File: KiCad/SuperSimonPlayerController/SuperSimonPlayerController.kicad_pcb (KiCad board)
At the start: 2 copper layers, 6 parts, among them U1 ESP32-S3-MINI-1-N8

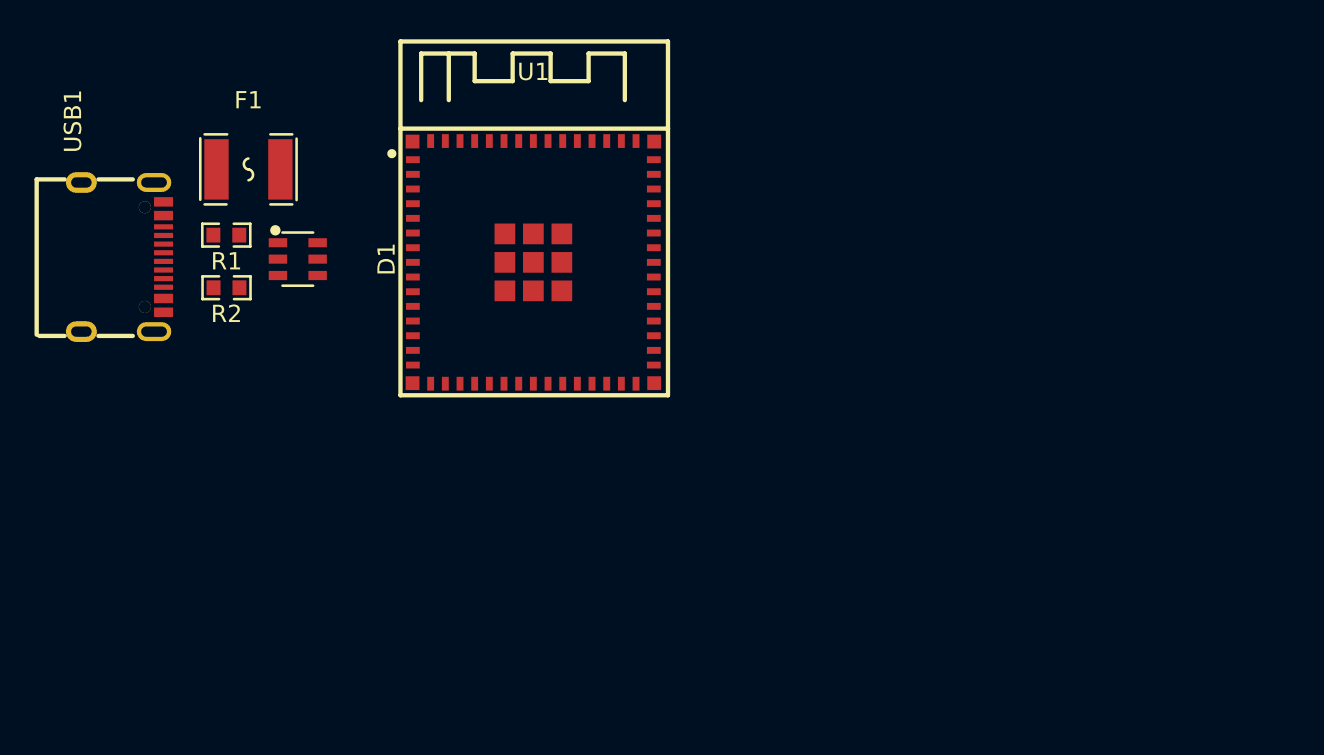
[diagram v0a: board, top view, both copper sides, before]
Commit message: Swapped to esp32-c3 with castallated pads, added some passives, created schematic sheet for the esp32
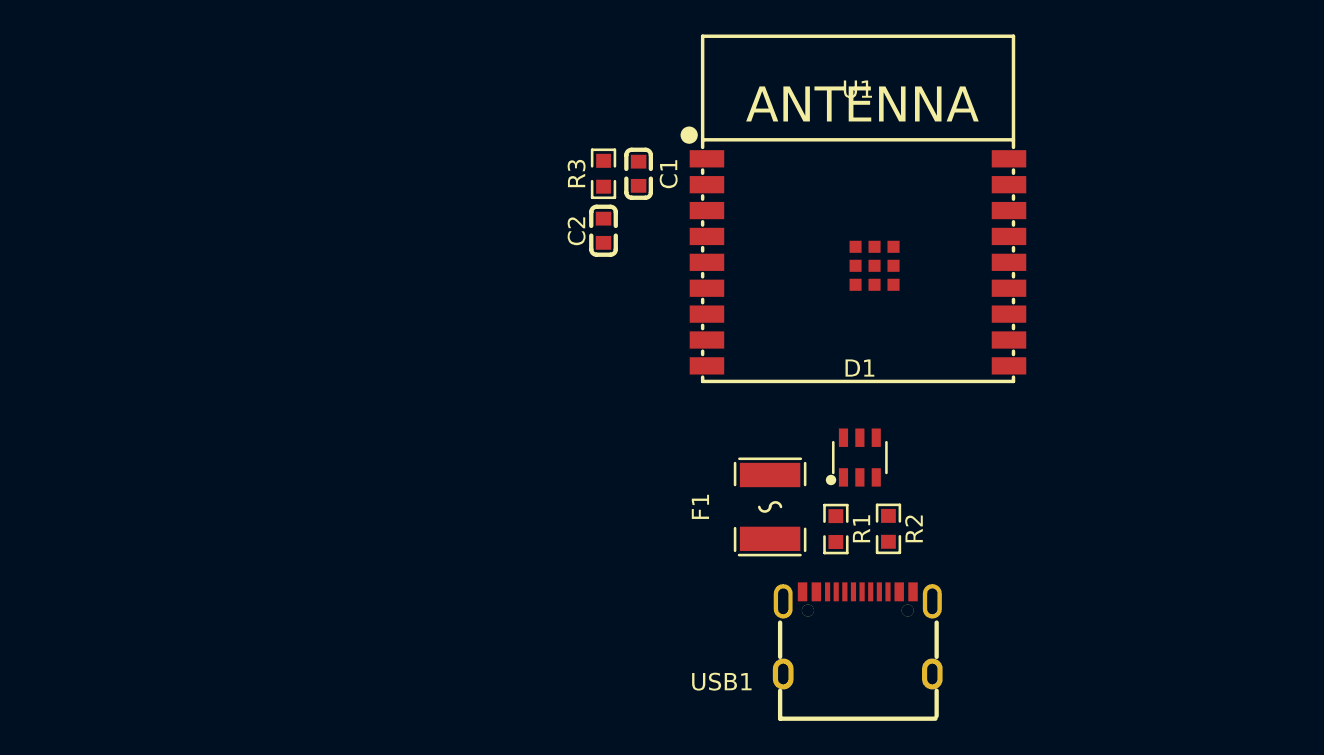
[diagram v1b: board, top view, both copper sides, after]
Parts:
- added C1: CL10A226MQ8NRNC, easyeda2kicad:C0603, F.Cu at (121.7, 92.5)
- added C2: CL10A226MQ8NRNC, easyeda2kicad:C0603, F.Cu at (119.6, 95.8)
- added R3: 0603WAF5101T5E, easyeda2kicad:R0603, F.Cu at (119.6, 92.5)
- U1: value ESP32-S3-MINI-1-N8 -> ESP32-C3-WROOM-02-N4(4MB); footprint easyeda2kicad:BULETM-SMD_ESP32-S3-MINI-1-N8 -> easyeda2kicad:BULETM-SMD_ESPRESSIF_ESP32-C3-WROOM-02-N4-4MB
- moved USB1 47.8 mm to (134.4, 119.1), turned to 0 degrees
- moved R2 40.8 mm to (136.1, 113.0), turned to 90 degrees
- moved R1 39.2 mm to (133.1, 113.0), turned to 90 degrees
- moved F1 36.0 mm to (129.3, 111.8), turned to 90 degrees
- moved D1 34.5 mm to (134.5, 108.9), turned to 0 degrees
- moved U1 18.8 mm to (134.4, 97.6)
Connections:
- U1 pad 1: unconnected-(U1-GND-Pad1) -> /ESP32-C3-WROOM-02-N4/3Vin
- U1 pad 13: unconnected-(U1-IO9-Pad13) -> /ESP32-C3-WROOM-02-N4/D-
- U1 pad 14: unconnected-(U1-IO10-Pad14) -> /ESP32-C3-WROOM-02-N4/D+
- U1 pad 19: unconnected-(U1-IO15-Pad19) -> /ESP32-C3-WROOM-02-N4/GND
- U1 pad 2: unconnected-(U1-GND-Pad2) -> /ESP32-C3-WROOM-02-N4/ENABLE
- U1 pad 9: unconnected-(U1-IO5-Pad9) -> /ESP32-C3-WROOM-02-N4/GND

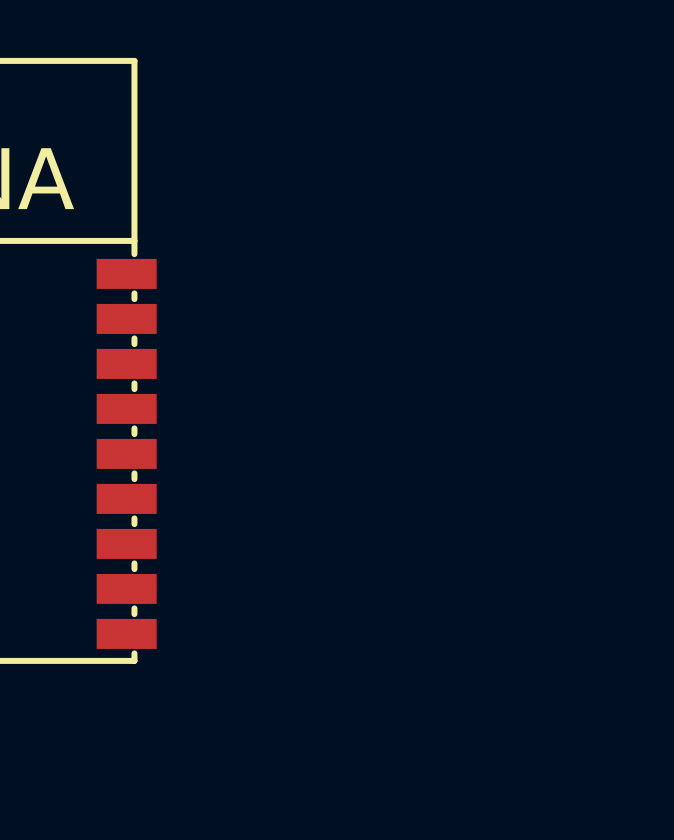
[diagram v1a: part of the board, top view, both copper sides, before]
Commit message: Added switches and boot-strapping pull-ups to esp32-c3
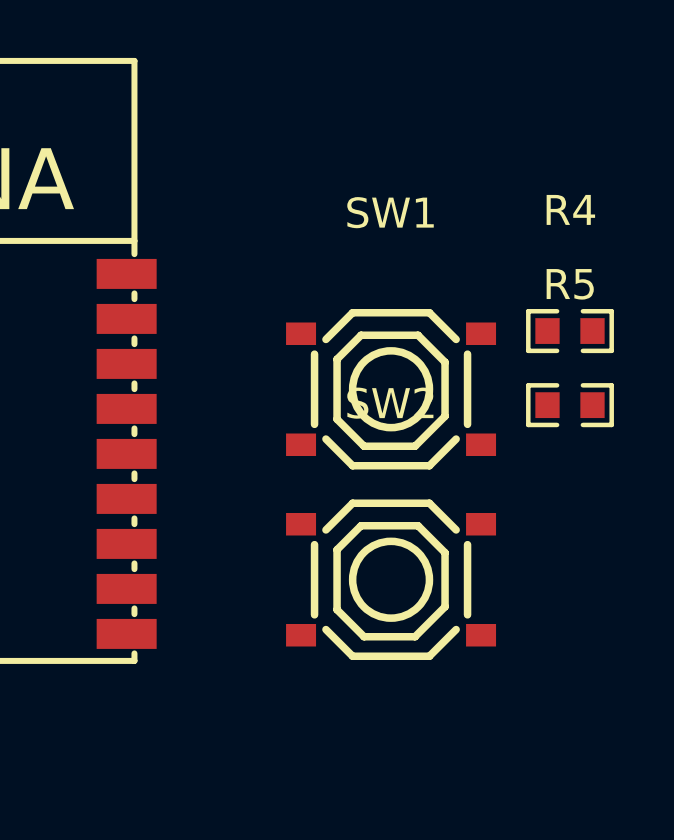
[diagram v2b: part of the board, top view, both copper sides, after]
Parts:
- added R4: 0603WAF5101T5E, easyeda2kicad:R0603, F.Cu at (157.9, 93.5)
- added R5: 0603WAF5101T5E, easyeda2kicad:R0603, F.Cu at (157.9, 96.0)
- added SW1: TS-1187A-B-A-B, easyeda2kicad:SW-SMD_4P-L5.1-W5.1-P3.70-LS6.5-TL_H1.5, F.Cu at (151.9, 95.4)
- added SW2: TS-1187A-B-A-B, easyeda2kicad:SW-SMD_4P-L5.1-W5.1-P3.70-LS6.5-TL_H1.5, F.Cu at (151.9, 101.8)
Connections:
- U1 pad 10: unconnected-(U1-IO10-Pad10) -> /ESP32-C3-WROOM-02-N4/D10/MOSI
- U1 pad 15: unconnected-(U1-IO3-Pad15) -> /ESP32-C3-WROOM-02-N4/D1/A1
- U1 pad 16: unconnected-(U1-IO2-Pad16) -> /ESP32-C3-WROOM-02-N4/D0/A0
- U1 pad 3: unconnected-(U1-IO4-Pad3) -> /ESP32-C3-WROOM-02-N4/D2/A2
- U1 pad 4: unconnected-(U1-IO5-Pad4) -> /ESP32-C3-WROOM-02-N4/D3/A3
- U1 pad 5: unconnected-(U1-IO6-Pad5) -> /ESP32-C3-WROOM-02-N4/D4/SDA
- U1 pad 6: unconnected-(U1-IO7-Pad6) -> /ESP32-C3-WROOM-02-N4/D5/SCL
- U1 pad 7: unconnected-(U1-IO8-Pad7) -> /ESP32-C3-WROOM-02-N4/D8/SCK
- U1 pad 8: unconnected-(U1-IO9-Pad8) -> /ESP32-C3-WROOM-02-N4/D9/MISO
